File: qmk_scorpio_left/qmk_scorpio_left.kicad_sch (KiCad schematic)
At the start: 42 parts, among them J1 USB_C_Receptacle_USB2.0, J2 Conn_01x05, J3 USB_C_Receptacle_USB2.0, Q3 MMUN2133LT1G, U1 STM32G474CETx, U2 PRTR5V0U2X, U3 XC6206PxxxMR-Regulator_Linear, U4 CR2013-MI2120, U5 PRTR5V0U2X

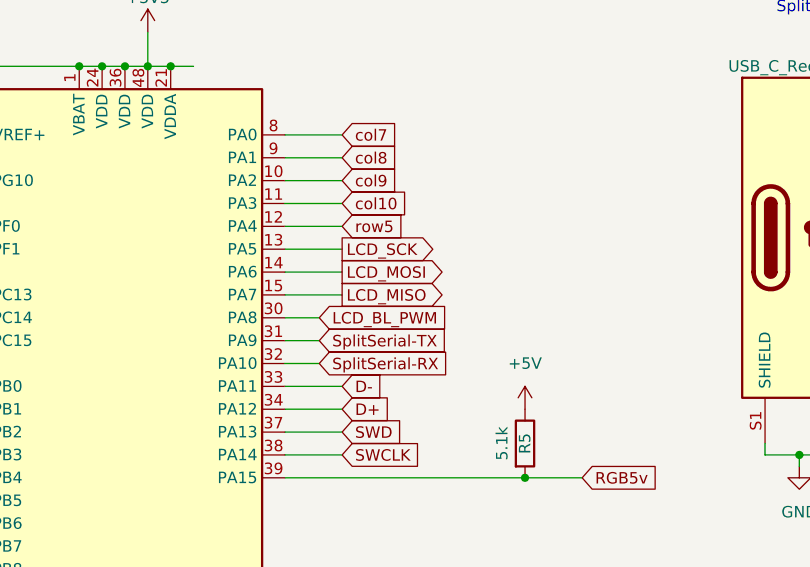
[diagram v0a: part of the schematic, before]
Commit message: pin corrections and updated rgb
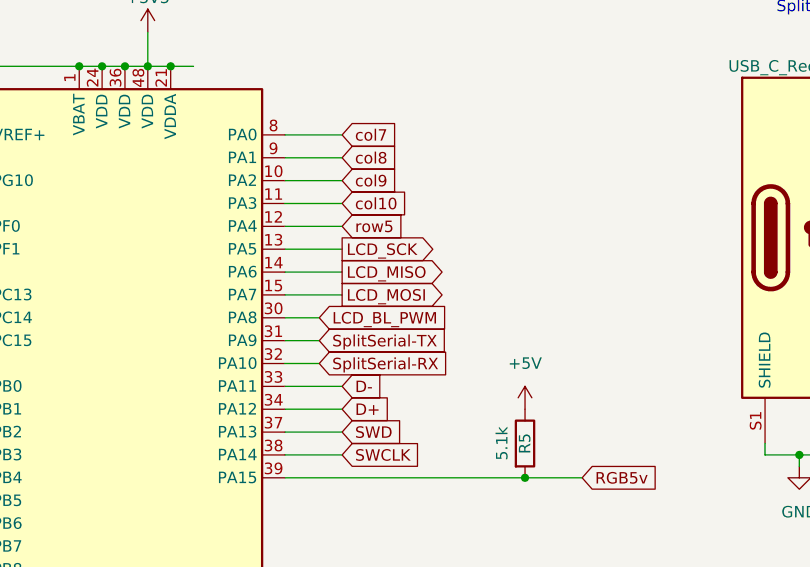
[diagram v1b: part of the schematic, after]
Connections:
- net LCD_MISO: now also U1.14 (PA6); no longer U1.15 (PA7)
- net LCD_MOSI: now also U1.15 (PA7); no longer U1.14 (PA6)
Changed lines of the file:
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@@
 		)
 	)
-	(global_label "LCD_MOSI"
+	(global_label "LCD_MISO"
 		(shape output)
 		(at 74.93 45.72 0)
@@
 		)
 	)
-	(global_label "LCD_MISO"
+	(global_label "LCD_MOSI"
 		(shape output)
 		(at 74.93 48.26 0)

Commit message: placed all components on board
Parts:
- removed H9: MountingHole_Pad, MountingHole:MountingHole_3.2mm_M3_DIN965_Pad, symbol Mechanical:MountingHole_Pad
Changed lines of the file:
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@@
 	)
 	(junction
-		(at 248.92 99.06)
-		(diameter 0)
-		(color 0 0 0 0)
-	)
-	(junction
 		(at 229.87 233.68)
 		(diameter 0)
@@
 	(wire
 		(pts
-			(xy 248.92 99.06) (xy 248.92 105.41)
-		)
-		(stroke
-			(width 0)
-			(type default)
-		)
-	)
-	(wire
-		(pts
-			(xy 248.92 105.41) (xy 252.73 105.41)
-		)
-		(stroke
-			(width 0)
-			(type default)
-		)
-	)
-	(wire
-		(pts
 			(xy 144.78 39.37) (xy 146.05 39.37)
 		)
@@
 					(unit 1)
 				)
-			)
-		)
-	)
-	(symbol
-		(lib_id "Mechanical:MountingHole_Pad")
-		(at 252.73 102.87 0)
-		(unit 1)
-		(exclude_from_sim yes)
-		(in_bom no)
-		(on_board yes)
-		(dnp no)
-		(fields_autoplaced yes)
-		(property "Reference" "H9"
-			(at 255.27 100.3299 0)
-			(effects
-				(font
-					(size 1.27 1.27)
-				)
-				(justify left)
-			)
-		)
-		(property "Value" "MountingHole_Pad"
-			(at 255.27 102.8699 0)
-			(effects
-				(font
-					(size 1.27 1.27)
-				)
-				(justify left)
-			)
-		)
-		(property "Footprint" "MountingHole:MountingHole_3.2mm_M3_DIN965_Pad"
-			(at 252.73 102.87 0)
-			(effects
-				(font
-					(size 1.27 1.27)
-				)
-				(hide yes)
-			)
-		)
-		(property "Datasheet" "~"
-			(at 252.73 102.87 0)
-			(effects
-				(font
-					(size 1.27 1.27)
-				)
-				(hide yes)
-			)
-		)
-		(property "Description" "Mounting Hole with connection"
-			(at 252.73 102.87 0)
-			(effects
-				(font
-					(size 1.27 1.27)
-				)
-				(hide yes)
-			)
-		)
-		(pin "1"
-		)
-		(instances
-			(project "hermod"
-				(path "/cb32b2da-a60d-4ed4-a57b-2c397f553171"
-					(reference "H9")
-					(unit 1)
-				)
